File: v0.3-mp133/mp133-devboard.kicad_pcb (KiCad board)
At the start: 4 copper layers, 39.9 x 57.9 mm, 146 parts, among them CON1 microSDCon_SMT_104031-0811, J1 Pins_02x40_P0.4mm_W3.0mm_SMT, J2 Pins_02x40_P0.4mm_W3.0mm_SMT, J3 USB-C_Receptacle_Molex_217179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, J4 Pins_02x04_RightAngle_P2.54mm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, J5 Conn_01x02, J6 Pins_02x05_P1.27mm_SMT, U13 NCP51460SN33, U14 DDR3L-RAM-4Gb_MT41K256M16TW, U15 AP6230xZ6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

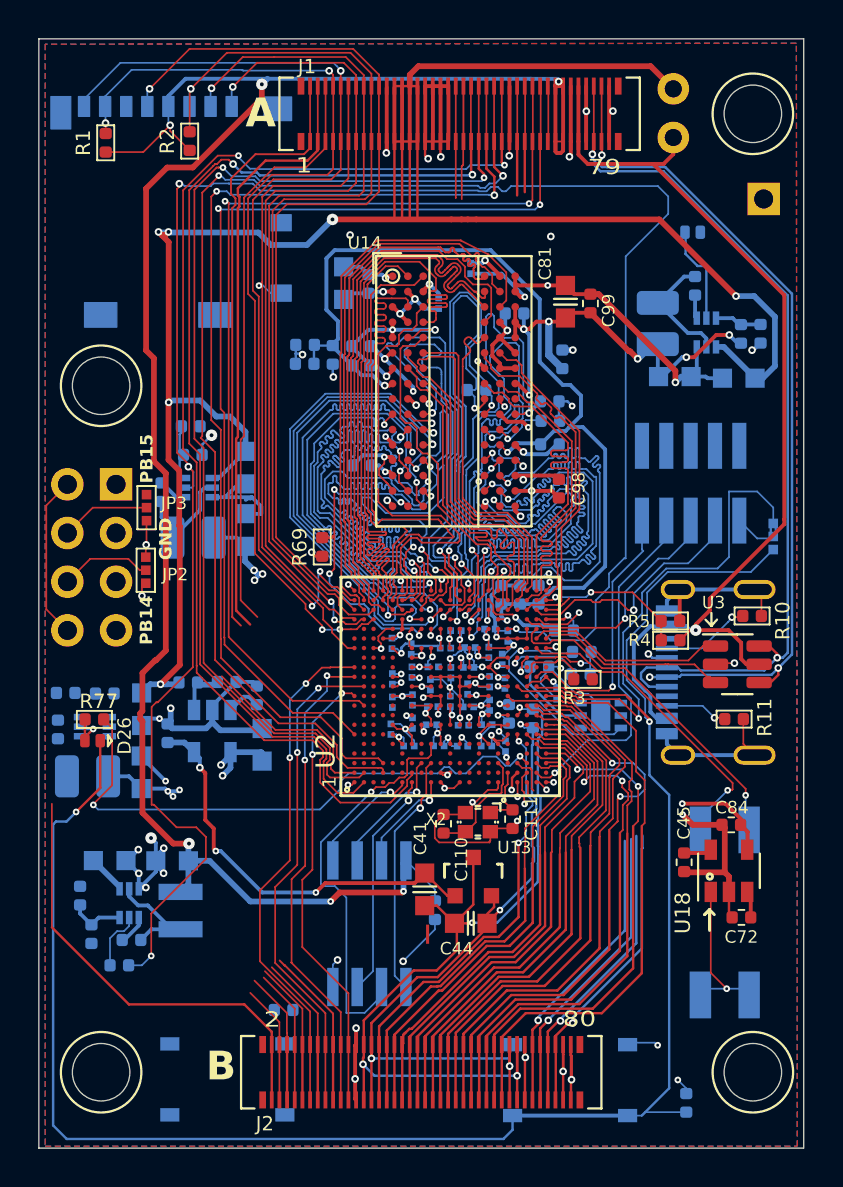
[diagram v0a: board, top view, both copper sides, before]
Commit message: mp133: WIP routing and pin assignment
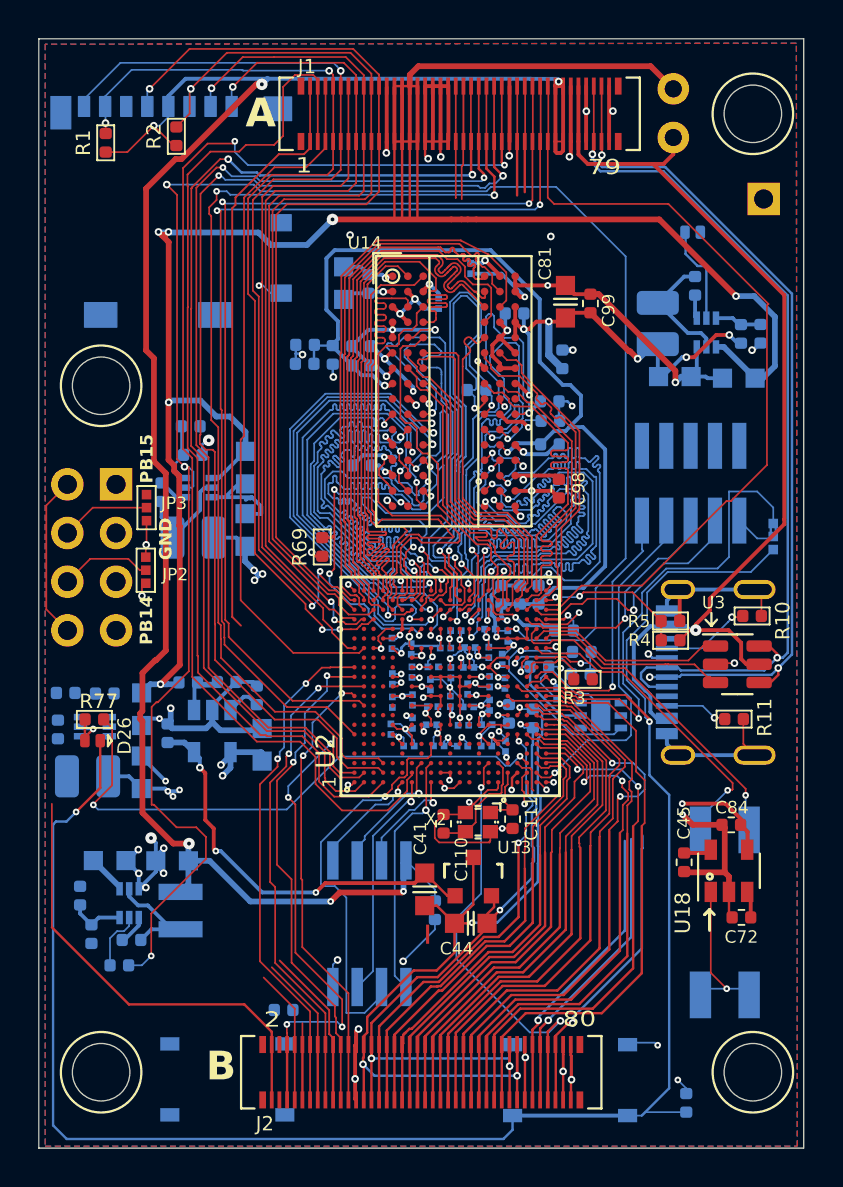
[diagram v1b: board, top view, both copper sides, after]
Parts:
- moved R2 0.74 mm to (196.3, 53.4)
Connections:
- J1 pad 3: Net-(J1-Pin_3) -> /PB8
- J1 pad 4: Net-(J1-Pin_3) -> /PB8
- J1 pad 5: Net-(J1-Pin_5) -> /PB15
- J1 pad 6: Net-(J1-Pin_5) -> /PB15
- J1 pad 63: Net-(J1-Pin_63) -> /PA10
- J1 pad 64: Net-(J1-Pin_63) -> /PA10
- J2 pad 10: /PD7 -> /PH8
- J2 pad 5: Net-(J2-Pin_5) -> /PA9
- J2 pad 6: Net-(J2-Pin_5) -> /PA9
- J2 pad 9: /PD7 -> /PH8
- U2 pad A2: /UART_TX -> /PA9
- U2 pad B15: unconnected-(U2A-PB15-PadB15) -> /PB15
- U2 pad C14: /DEBUG0 -> unconnected-(U2A-PB3-PadC14)
- U2 pad E3: unconnected-(U2B-PH8-PadE3) -> /PH8
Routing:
- net /PB8: track 0.00 -> 53.5 mm
- net /PA10: track 1.47 -> 42.7 mm
- net /PB15: track 0.00 -> 37.3 mm
- net Net-(J1-Pin_3): track 31.5 -> 0.00 mm
- net Net-(J1-Pin_5): track 30.9 -> 0.00 mm
- net /PA9: track 0.00 -> 26.4 mm, vias 0 -> 4
- net /UART_TX: track 9.86 -> 0.00 mm
- net /PD7: track 8.39 -> 0.00 mm, vias 1 -> 0
- net Net-(J2-Pin_5): track 7.03 -> 0.00 mm
- net /PH3: track 15.8 -> 22.7 mm, vias 1 -> 2
- net Net-(J2-Pin_3): track 6.31 -> 0.00 mm
- net /PWR_ON: track 103.3 -> 98.8 mm
- net /PH8: track 0.00 -> 4.10 mm
- net VDD: track 71.1 -> 74.6 mm
- net Net-(J1-Pin_63): track 2.89 -> 0.00 mm
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
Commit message: mp133: routing and pin assignment
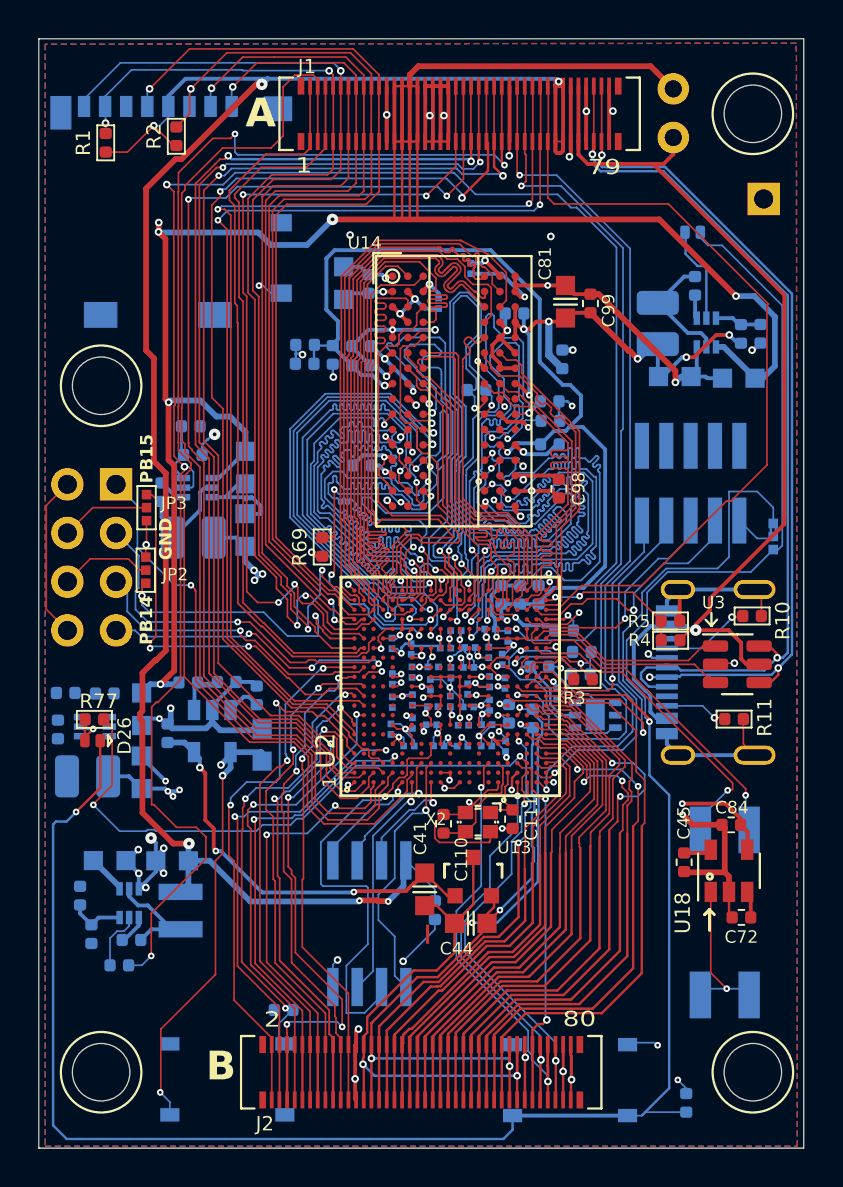
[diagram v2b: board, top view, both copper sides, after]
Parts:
- moved U20 0.29 mm to (218.2, 83.6)
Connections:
- J1 pad 1: Net-(J1-Pin_1) -> /PB4
- J1 pad 2: Net-(J1-Pin_1) -> /PB4
- J1 pad 39: Net-(J1-Pin_39) -> /PB14
- J1 pad 40: Net-(J1-Pin_39) -> /PB14
- J1 pad 41: Net-(J1-Pin_41) -> /PD3
- J1 pad 42: Net-(J1-Pin_41) -> /PD3
- J1 pad 55: Net-(J1-Pin_55) -> /PA11
- J1 pad 56: Net-(J1-Pin_55) -> /PA11
- J1 pad 57: Net-(J1-Pin_57) -> /PE5
- J1 pad 58: Net-(J1-Pin_57) -> /PE5
- J2 pad 1: Net-(J2-Pin_1) -> /PE12
- J2 pad 13: Net-(J2-Pin_13) -> /PB6
- J2 pad 14: Net-(J2-Pin_13) -> /PB6
- J2 pad 17: Net-(J2-Pin_17) -> /PE13
- J2 pad 18: Net-(J2-Pin_17) -> /PE13
- J2 pad 2: Net-(J2-Pin_1) -> /PE12
- J2 pad 3: Net-(J2-Pin_3) -> /PD14
- J2 pad 4: Net-(J2-Pin_3) -> /PD14
- J2 pad 69: Net-(J2-Pin_69) -> /PG2
- J2 pad 7: Net-(J2-Pin_7) -> /PH14
- J2 pad 70: Net-(J2-Pin_69) -> /PG2
- J2 pad 71: Net-(J2-Pin_71) -> /PD7
- J2 pad 72: Net-(J2-Pin_71) -> /PD7
- J2 pad 75: Net-(J2-Pin_75) -> /PG12
- J2 pad 76: Net-(J2-Pin_75) -> /PG12
- J2 pad 8: Net-(J2-Pin_7) -> /PH14
- J4 pad 1: /UART_TX -> /UART7_TX
- J4 pad 3: /UART_RX -> /UART7_RX
- U2 pad A16: unconnected-(U2B-PF0-PadA16) -> /DEBUG3
- U2 pad A7: /PG0 -> /DFU_BOOT
- U2 pad B10: /PG4 -> /DEBUG2
- U2 pad B13: unconnected-(U2A-PB5-PadB13) -> /DEBUG0
- U2 pad B16: unconnected-(U2A-PB14-PadB16) -> /PB14
- U2 pad B4: /UART_RX -> unconnected-(U2A-PA15-PadB4)
- U2 pad B8: unconnected-(U2B-PH14-PadB8) -> /PH14
- U2 pad C1: unconnected-(U2A-PB6-PadC1) -> /PB6
- U2 pad C13: /PC7 -> /DEBUG1
- U2 pad C14: unconnected-(U2A-PB3-PadC14) -> /UART7_RX
- U2 pad C16: /DEBUG1 -> /PB4
- U2 pad C4: unconnected-(U2A-PD14-PadC4) -> /PD14
- U2 pad E2: unconnected-(U2B-PH2-PadE2) -> /UART7_TX
- U2 pad W10: /DEBUG1 -> /PE5
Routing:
- net /PD3: track 0.00 -> 58.4 mm, vias 0 -> 2
- net /PE5: track 0.00 -> 46.4 mm, vias 0 -> 2
- net /PB14: track 0.00 -> 45.4 mm, vias 0 -> 4
- net /PA11: track 0.68 -> 45.5 mm, vias 1 -> 2
- net /PB4: track 0.00 -> 38.9 mm
- net Net-(J1-Pin_1): track 30.8 -> 0.00 mm
- net /PE12: track 0.00 -> 29.1 mm, vias 0 -> 2
- net /UART7_TX: track 0.00 -> 28.9 mm, vias 0 -> 1
- net /PD14: track 0.00 -> 25.8 mm, vias 0 -> 2
- net /PH14: track 0.00 -> 25.3 mm, vias 0 -> 2
- net /PE13: track 0.00 -> 24.9 mm, vias 0 -> 2
- net Net-(J2-Pin_1): track 23.8 -> 0.00 mm
- net /DFU_BOOT: track 0.00 -> 23.7 mm, vias 0 -> 3
- net /PB6: track 0.00 -> 22.6 mm, vias 0 -> 2
- net /PD7: track 0.00 -> 21.4 mm, vias 0 -> 2
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
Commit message: mp133: completed routing
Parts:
- added D1: BAT54LP, 4ms_Diode:DFN-1006-2, B.Cu at (190.9, 96.6)
- added R6: 10k_0402, 4ms_Resistor:R_0402, B.Cu at (193.3, 96.5)
- moved R76 48.7 mm to (222.2, 57.3), turned to 0 degrees
- moved R60 1.24 mm to (197.0, 80.6)
- moved C192 0.40 mm to (210.0, 61.7)
- moved C75 0.25 mm to (200.8, 82.5)
- moved C46 0.14 mm to (196.0, 84.5)
- moved U19 0.12 mm to (198.3, 84.4)
- moved C88 0.10 mm to (200.9, 85.1)
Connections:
- U16 pad 5: /PWR_ONRST -> /PWR_ONRST2
- U2 pad AA13: /USB2_DP -> unconnected-(U2D-USB_DP2-PadAA13)
- U2 pad B14: /PC6 -> unconnected-(U2A-PC6-PadB14)
- U2 pad B17: /PE3 -> unconnected-(U2B-PE3-PadB17)
- U2 pad B6: /PE0 -> unconnected-(U2B-PE0-PadB6)
- U2 pad C10: /PE10 -> unconnected-(U2B-PE10-PadC10)
- U2 pad C17: /PG6 -> unconnected-(U2B-PG6-PadC17)
- U2 pad C6: /PB7 -> unconnected-(U2A-PB7-PadC6)
- U2 pad D6: /PD10 -> unconnected-(U2A-PD10-PadD6)
- U2 pad E13: /PB10 -> unconnected-(U2A-PB10-PadE13)
- U2 pad F2: /PG9 -> unconnected-(U2B-PG9-PadF2)
- U2 pad F3: /PD11 -> unconnected-(U2A-PD11-PadF3)
- U2 pad F4: /PA12 -> unconnected-(U2A-PA12-PadF4)
- U2 pad G3: /PG5 -> unconnected-(U2B-PG5-PadG3)
- U2 pad H2: /PE4 -> unconnected-(U2B-PE4-PadH2)
- U2 pad H4: /PG15 -> unconnected-(U2B-PG15-PadH4)
- U2 pad J2: /PD13 -> unconnected-(U2A-PD13-PadJ2)
- U2 pad K3: / PH11 -> unconnected-(U2B-PH11-PadK3)
- U2 pad N1: /PE2 -> unconnected-(U2B-PE2-PadN1)
- U2 pad N3: /PH6 -> unconnected-(U2B-PH6-PadN3)
- U2 pad P2: /PA8 -> unconnected-(U2A-PA8-PadP2)
- U2 pad R1: /PG1 -> unconnected-(U2B-PG1-PadR1)
- U2 pad T2: /PE6 -> unconnected-(U2B-PE6-PadT2)
- U2 pad W1: /PG3 -> unconnected-(U2B-PG3-PadW1)
- U2 pad W4: /PF13 -> unconnected-(U2B-PF13-PadW4)
- U2 pad W5: /PC0 -> unconnected-(U2A-PC0-PadW5)
- U2 pad W8: /PB0 -> unconnected-(U2A-PB0-PadW8)
- U2 pad Y13: /USB2_DN -> unconnected-(U2D-USB_DM2-PadY13)
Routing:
- net +5V: track 147.3 -> 219.5 mm, vias 9 -> 10
- net VDD: track 94.3 -> 153.9 mm, vias 18 -> 21
- net VDD_CORE: track 43.7 -> 58.7 mm
- net +3V3: track 107.0 -> 120.4 mm
- net GND: track 248.6 -> 260.9 mm, vias 89 -> 94
- net VDD_CPU: track 31.3 -> 43.4 mm
- net /PWR_ONRST2: track 0.00 -> 6.08 mm
- net Net-(U21-SW): track 0.00 -> 5.95 mm
- net /NRST: track 118.3 -> 112.8 mm
- net /PWR_ON: track 98.7 -> 102.8 mm, vias 4 -> 6
- net VDD_DDR: track 63.5 -> 67.5 mm
- net Net-(U21-FB): track 0.00 -> 2.46 mm
- net /PA10: track 42.7 -> 44.8 mm
- net /PWR_ONRST: track 8.31 -> 6.36 mm
- net Net-(U21-BST): track 0.00 -> 1.61 mm
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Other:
- board text added: "DBG2"
- board text added: "DBG3"
- board text removed: "PB14"
- board text removed: "PB15"
